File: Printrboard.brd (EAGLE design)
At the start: 100.1 x 61 mm, 122 parts, among them J1 MICROSD, J3 ATX, Q1 RFP30N06LE, Q2 RFP30N06LE, Q3 RFP30N06LE, U1 LM2841, U2 A4982, U3 A4982, U4 A4982, U5 A4982, U6 AT90USB1286, U7 AP7313, U8 TXB0104, X1 16MHz, X2 USB-MICROB

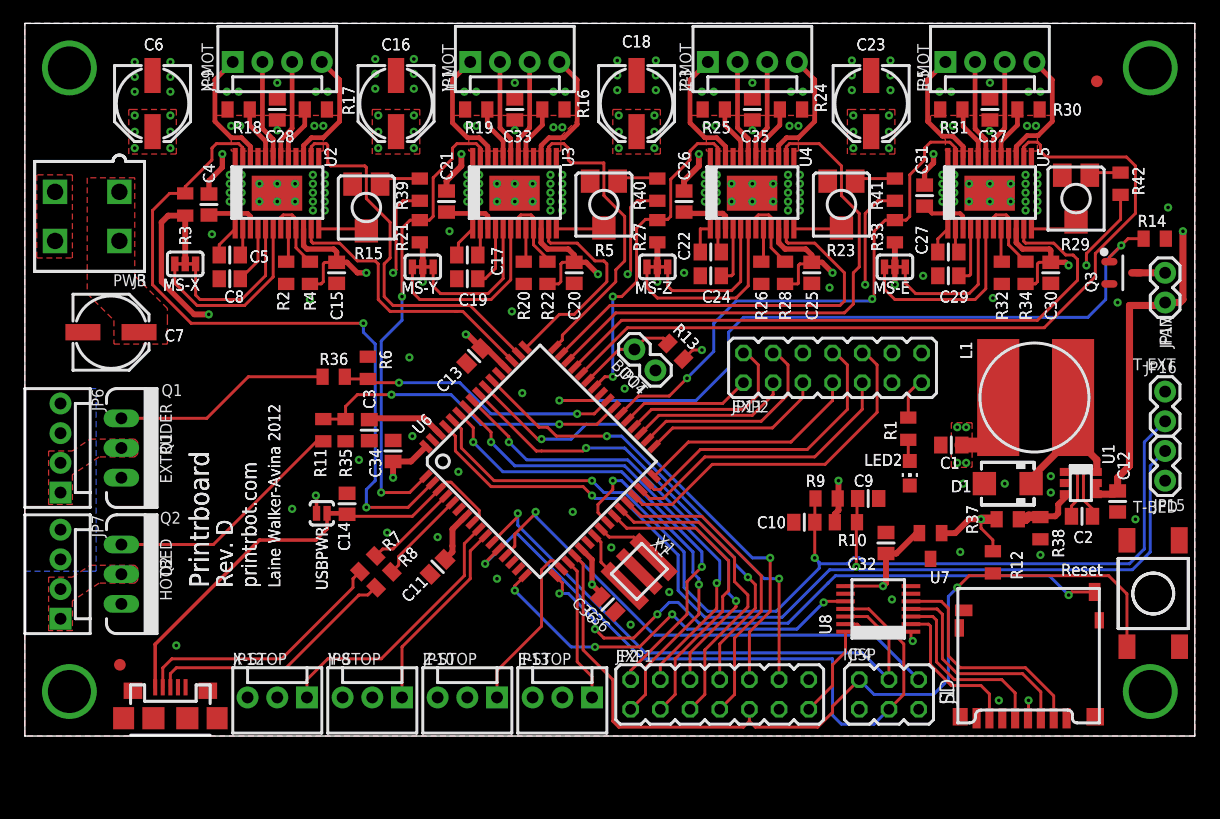
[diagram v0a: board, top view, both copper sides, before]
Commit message: Update files for Rev F
Changed heatbed connector to 5mm pitch screw terminal
Removed E-STOP connector
Changed Y-STOP pin
Moved former Y-STOP pin to SD interface to fix a limitation of the SPI ctlr
Added I2C connector
Replaced trimpots with 4-channel I2C DAC
Added polyfuse and reverse protection diode to fan circuit
Added more empty space around fan connector
Made ICSP and EXP1 connector pins share a 0.1" grid
Removed reset signal from EXP1, and replaced it with GPIO
Changed input PWR connector to a 6-pin one from the same family
Removed stop layer from several vias for future bed-of-nails tester
Change to through-hole mount microUSB connector
Added USB TVS diode pack to protect USB controller from ESD
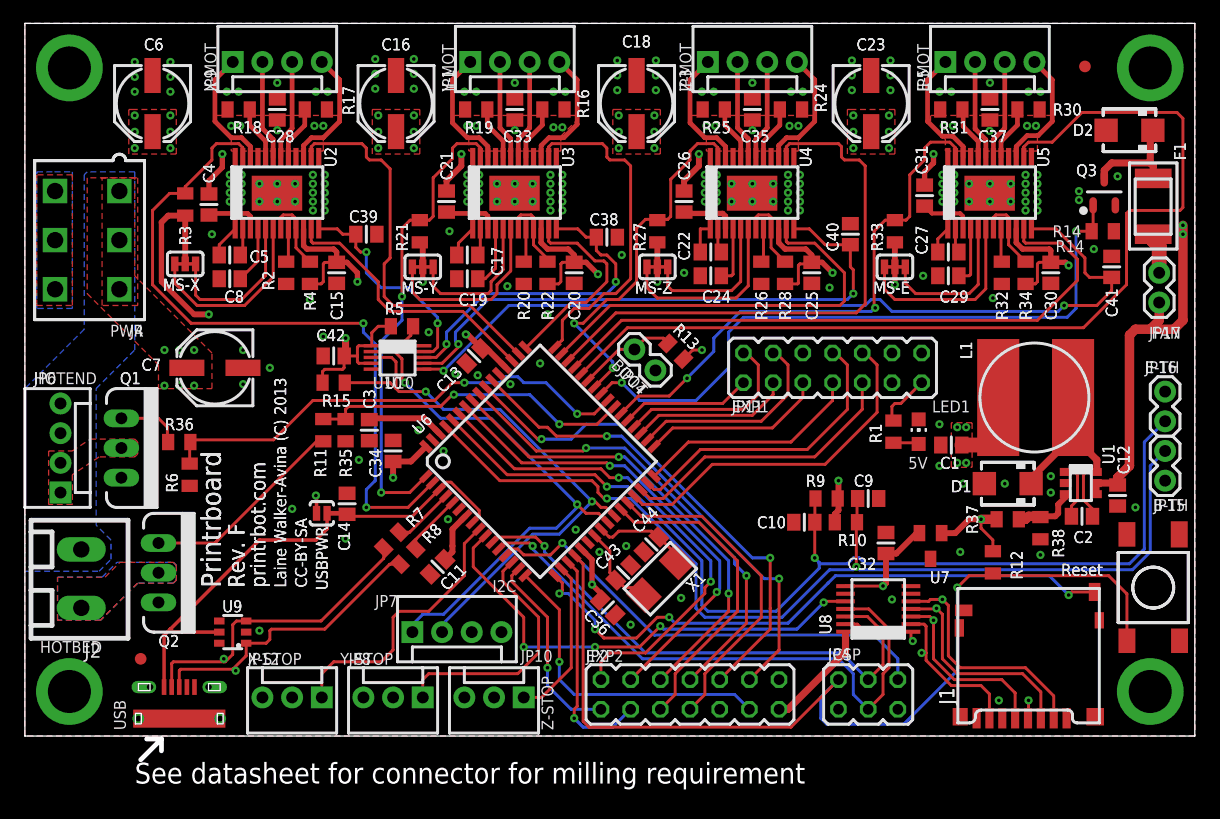
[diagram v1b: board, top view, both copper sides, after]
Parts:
- removed JP13: E-STOP, SparkFun:MOLEX-1X3
- removed LED2: PWR, led:CHIP-LED0805
- removed R23, R29: 10k, printrbot:RTRIM-ST4ETB
- removed R39, R40, R41, R42: 20k, ipc-7351-resistor:RESC2012X70N
- removed X2: USB-MICROB, printrbot:USB-MICROB
- added C38, C39, C40, C41, C42: 0.1uF, ipc-7351-capacitor:CAPC2012X145AN
- added C43, C44: 10pF, ipc-7351-capacitor:CAPC2012X145AN
- added D2: (no value), printrbot:SMA
- added F1: (no value), printrbot:MINISMDC
- added J2: (no value), printrbot:PHOENIX-5MM-2POS
- added J4: PCIE, printrbot:5566-6
- added LED1: PWR, led:CHIP-LED0805
- added U10: MCP4728, printrbot:MSOP10
- added U9: PRTR5V0U4D, printrbot:SOT23-6
- J3: value ATX -> USB-MICRO-PTH; device printrbot:5566-4 -> printrbot:USB-MICROB-PTH
- JP7: value HOTBED -> I2C
- R15, R5: value 10k -> 4.7k; device printrbot:RTRIM-ST4ETB -> ipc-7351-resistor:RESC2012X70N
- X1: device printrbot:AWSCR -> printrbot:NDK-XTAL
- moved J3 42.9 mm to (13.2, 2.29), turned to 0 degrees
- moved JP7 30.1 mm to (33.1, 8.89), turned to 0 degrees
- moved R5 20.2 mm to (32.3, 35.1)
- moved R6 17.8 mm to (14.1, 22.4), turned to 270 degrees
- moved R15 15.2 mm to (26.4, 30.2)
- moved R36 14.3 mm to (13.2, 25.1)
- moved C7 9.40 mm to (16.3, 31.5), turned to 180 degrees
- moved Q3 7.10 mm to (92.3, 46.5), turned to 90 degrees
- moved R14 4.49 mm to (92.2, 43.2)
- moved Q2 3.18 mm to (11.4, 14.0)
- moved R7 2.87 mm to (31.4, 16.8)
- moved R8 2.86 mm to (32.8, 15.4)
- moved JP2 2.54 mm to (56.9, 3.56)
- moved JP10 2.29 mm to (42.7, 3.30)
- moved X1 1.90 mm to (54.4, 13.5)
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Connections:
- removed net E-STOP: JP13.1, U6.19
- removed net N$18: R15.W, U2.12
- removed net N$33: R5.W, U3.12
- removed net N$48: R23.W, U4.12
- removed net N$6: JP17.2, Q3.3
- removed net N$63: R29.W, U5.12
- removed net N$69: R15.1, R39.1
- removed net N$74: R29.1, R42.1
- removed net N$78: R23.1, R41.1
- removed net N$8: R40.1, R5.1
- removed net PD0-SCL: JP2.1, U6.25
- removed net PD1-SDA: JP2.3, U6.26
- new net MCU_DN: J3.D-, R7.1, U9.3
- new net MCU_DP: J3.D+, R8.1, U9.1
- new net PB5: JP2.1, U6.15
- new net PB6: JP2.11, U6.16
- new net PE5: JP2.3, U6.19
- new net SCL: JP7.1, R5.1, U10.2, U6.25
- new net SDA: JP7.2, R15.1, U10.3, U6.26
- new net VREF_E: C41.1, U10.6, U5.12
- new net VREF_X: C39.1, U10.9, U2.12
- new net VREF_Y: C38.1, U10.8, U3.12
- new net VREF_Z: C40.1, U10.7, U4.12
- net !RESET: no longer JP2.9
- net +5V: now also C42.2, JP7.4, R15.2, R5.2, U10.1, U10.4; no longer JP13.2, R39.2, R40.2, R41.2, R42.2
- net 12V: now also J2.P$1, J4.1, J4.2, J4.3; no longer J3.1, J3.2, JP7.3, JP7.4
- net GND: now also C38.2, C39.2, C40.2, C41.2, C42.1, C43.1, C44.1, D2.A, J3.GND, J3.GND1, J3.GND2, J3.GND3, J3.GND4, J3.GND5, J4.4, J4.5, J4.6, JP7.3, LED1.C, U10.10, U9.2; no longer J3.3, J3.4, JP13.3, LED2.C, R15.2, R23.2, R29.2, R5.2, X1.GND, X2.GND, X2.MT1, X2.MT2, X2.MT3, X2.MT4, X2.MT5, X2.MT6
- net HOTBED-GND: now also J2.P$2; no longer JP7.1, JP7.2
- net N$1: now also LED1.A; no longer LED2.A
- net N$2: now also D2.C, F1.P$2, Q3.3; no longer R7.1, X2.D-
- net N$5: now also F1.P$1, JP17.2; no longer R8.1, X2.D+
- net SDCS: now also U6.10; no longer U6.16
- net VBUS: now also J3.VBUS, U9.5; no longer X2.VBUS
- net XTAL1: now also C44.2, X1.P$1; no longer X1.IN
- net XTAL2: now also C43.2, X1.P$2; no longer X1.OUT
- net Y-STOP: now also U6.14; no longer U6.10
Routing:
- net VREF_E: track 0.00 -> 73.2 mm, vias 0 -> 2
- net SDA: track 0.00 -> 50.1 mm, vias 0 -> 2
- net VREF_Z: track 0.00 -> 50.0 mm, vias 0 -> 2
- net SCL: track 0.00 -> 49.3 mm, vias 0 -> 2
- net PD0-SCL: track 29.9 -> 0.00 mm, vias 2 -> 0
- net VREF_Y: track 0.00 -> 28.6 mm, vias 0 -> 2
- net PB6: track 0.00 -> 27.4 mm, vias 0 -> 1
- net MCU_DN: track 0.00 -> 26.5 mm, vias 0 -> 1
- net PD1-SDA: track 26.5 -> 0.00 mm
- net MCU_DP: track 0.00 -> 25.5 mm, vias 0 -> 1
- net PE5: track 0.00 -> 19.5 mm, vias 0 -> 1
- net VREF_X: track 0.00 -> 18.9 mm, vias 0 -> 2
- net N$5: track 21.8 -> 3.51 mm
- net !HOTEND: track 24.7 -> 42.2 mm
- net PB5: track 0.00 -> 16.9 mm, vias 0 -> 1
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- added copper zone on layer 16, net HOTBED-GND
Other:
- board size 100.1 x 61 mm -> 100.1 x 63 mm
- board text added: "/home/ceriand/Downloads/pbrd-logo.bmp"
- board text added: "5V"
- board text added: "B-TH"
- board text added: "C38"
- board text added: "C39"
- board text added: "C40"
- board text added: "C41"
- board text added: "C42"
- board text added: "C43"
- board text added: "C44"
- board text added: "CC-BY-SA"
- board text added: "D2"
- board text added: "E-TH"
- board text added: "F1"
- board text added: "HOTEND"
- board text added: "I2C"
- board text added: "J1"
- board text added: "Laine Walker-Avina (C) 2013"
- board text added: "Rev. F"
- board text added: "See datasheet for connector for milling requirement"
- board text added: "U10"
- board text added: "U9"
- board text added: "USB"
- board text removed: "E-STOP"
- board text removed: "EXTRUDER"
- board text removed: "LED2"
- board text removed: "Laine Walker-Avina 2012"
- board text removed: "R23"
- board text removed: "R29"
- board text removed: "R39"
- board text removed: "R40"
- board text removed: "R41"
- board text removed: "R42"
- board text removed: "Rev. D"
- board text removed: "SD"
- board text removed: "T-BED"
- board text removed: "T-EXT"

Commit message: Manufacturability changes
Added some pin 1 indicators
Added test point for VBUS signal
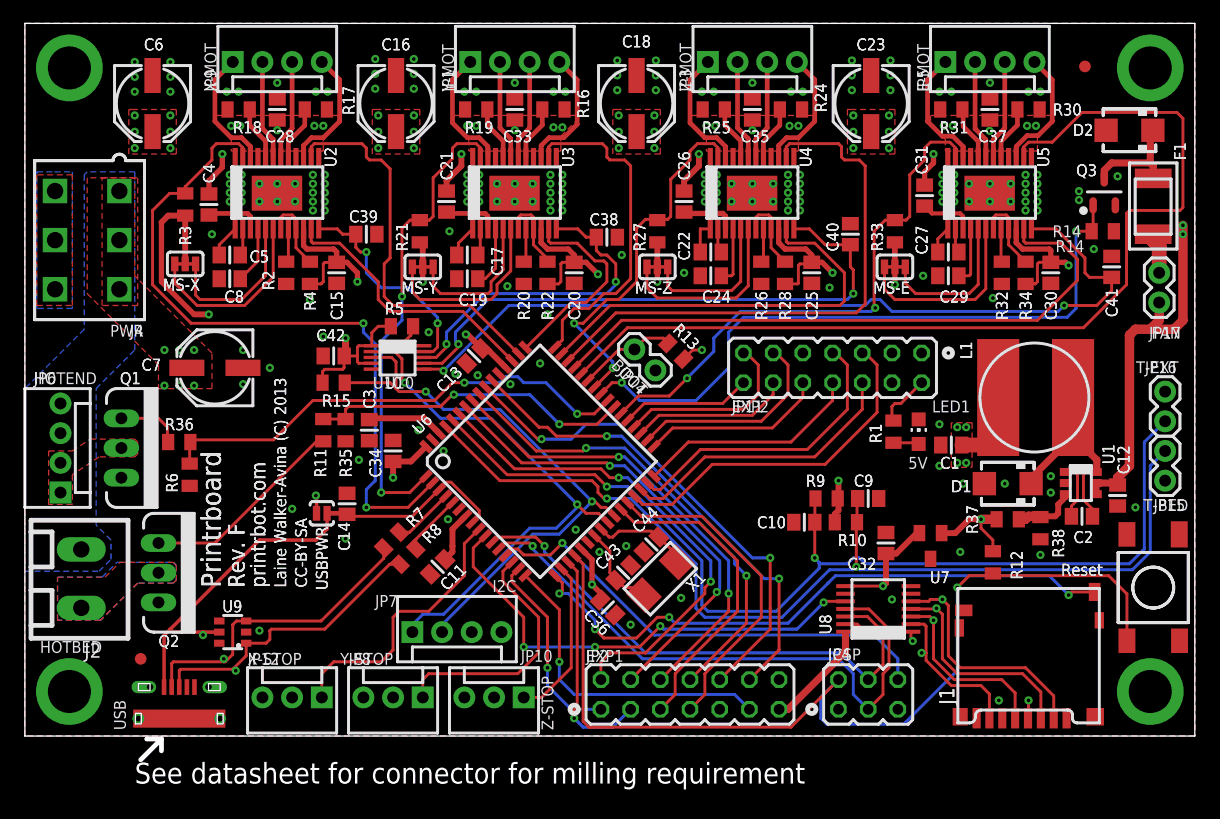
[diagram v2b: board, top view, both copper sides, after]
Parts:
- JP11: value EXP -> EXP2
- JP2: value EXP -> EXP1
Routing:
- net VBUS: track 44.4 -> 44.7 mm, vias 0 -> 1
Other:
- board text added: "T-BED"
- board text added: "T-EXT"
- board text removed: "B-TH"
- board text removed: "E-TH"
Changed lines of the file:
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@@
 <layer number="14" name="Route14" color="1" fill="6" visible="no" active="no"/>
 <layer number="15" name="Route15" color="4" fill="6" visible="no" active="no"/>
-<layer number="16" name="Bottom" color="1" fill="1" visible="yes" active="yes"/>
+<layer number="16" name="Bottom" color="1" fill="1" visible="no" active="yes"/>
 <layer number="17" name="Pads" color="2" fill="1" visible="yes" active="yes"/>
 <layer number="18" name="Vias" color="2" fill="1" visible="yes" active="yes"/>
@@
 <wire x1="60.706" y1="5.715" x2="61.087" y2="6.096" width="0.254" layer="121"/>
 <wire x1="63.246" y1="5.715" x2="63.627" y2="6.096" width="0.254" layer="121"/>
-<text x="48.006" y="6.35" size="1.016" layer="121" ratio="25">EXP2</text>
+<text x="48.006" y="6.35" size="1.016" layer="121" ratio="25">EXP1</text>
 <wire x1="57.15" y1="60.706" x2="57.15" y2="55.118" width="0.254" layer="121"/>
 <wire x1="67.31" y1="60.706" x2="67.31" y2="55.118" width="0.254" layer="121"/>
@@
 <wire x1="65.278" y1="29.337" x2="64.897" y2="28.956" width="0.254" layer="121"/>
 <wire x1="62.738" y1="29.337" x2="62.357" y2="28.956" width="0.254" layer="121"/>
-<text x="60.452" y="27.686" size="1.016" layer="121" ratio="25">EXP1</text>
+<text x="60.452" y="27.686" size="1.016" layer="121" ratio="25">EXP2</text>
 <wire x1="26.67" y1="0.254" x2="26.67" y2="5.842" width="0.254" layer="121"/>
 <wire x1="19.05" y1="0.254" x2="19.05" y2="5.842" width="0.254" layer="121"/>
@@
 <wire x1="96.266" y1="23.749" x2="96.266" y2="25.019" width="0.254" layer="121"/>
 <wire x1="98.171" y1="20.574" x2="96.901" y2="20.574" width="0.254" layer="121"/>
-<text x="99.5172" y="20.2692" size="1.016" layer="121" ratio="25" rot="R180">B-TH</text>
+<text x="99.5172" y="20.2692" size="1.016" layer="121" ratio="25" rot="R180">T-BED</text>
 <wire x1="96.266" y1="26.289" x2="96.266" y2="27.559" width="0.254" layer="121"/>
 <wire x1="96.266" y1="27.559" x2="96.901" y2="28.194" width="0.254" layer="121"/>
@@
 <wire x1="98.806" y1="27.559" x2="98.806" y2="26.289" width="0.254" layer="121"/>
 <wire x1="96.901" y1="30.734" x2="98.171" y2="30.734" width="0.254" layer="121"/>
-<text x="95.8088" y="31.0388" size="1.016" layer="121" ratio="25">E-TH</text>
+<text x="95.0468" y="31.0388" size="1.016" layer="121" ratio="25">T-EXT</text>
 <wire x1="95.758" y1="36.449" x2="95.758" y2="37.719" width="0.254" layer="121"/>
 <wire x1="95.758" y1="37.719" x2="96.393" y2="38.354" width="0.254" layer="121"/>
@@
 <wire x1="11.684" y1="-0.254" x2="11.684" y2="-1.27" width="0.4064" layer="46"/>
 <text x="8.636" y="0.508" size="1.016" layer="121" ratio="20" rot="R90">USB</text>
+<circle x="46.99" y="2.286" radius="0.359209375" width="0.4064" layer="121"/>
+<circle x="78.994" y="32.766" radius="0.359209375" width="0.4064" layer="121"/>
+<circle x="67.31" y="2.286" radius="0.359209375" width="0.4064" layer="121"/>
 </plain>
 <attributes>
@@
 <attribute name="VALUE" x="43.942" y="7.747" size="1.27" layer="27" rot="R180"/>
 </element>
-<element name="JP2" library="printrbot" package="JP7Q" value="EXP" x="56.896" y="3.556" smashed="yes">
+<element name="JP2" library="printrbot" package="JP7Q" value="EXP1" x="56.896" y="3.556" smashed="yes">
 <attribute name="NAME" x="48.006" y="6.35" size="1.016" layer="25" ratio="20"/>
 <attribute name="VALUE" x="48.006" y="-2.159" size="1.27" layer="27" ratio="10"/>
 </element>
-<element name="JP11" library="printrbot" package="JP7Q" value="EXP" x="69.088" y="31.496" smashed="yes" rot="R180">
+<element name="JP11" library="printrbot" package="JP7Q" value="EXP2" x="69.088" y="31.496" smashed="yes" rot="R180">
 <attribute name="NAME" x="60.452" y="27.686" size="1.016" layer="25" ratio="20"/>
 <attribute name="VALUE" x="77.978" y="37.211" size="1.27" layer="27" ratio="10" rot="R180"/>
@@
 <contactref element="J3" pad="VBUS"/>
 <contactref element="U9" pad="5"/>
-<wire x1="16.63" y1="8.89" x2="12.7" y2="8.89" width="0.3048" layer="1"/>
+<wire x1="16.63" y1="8.89" x2="15.24" y2="8.89" width="0.3048" layer="1"/>
+<wire x1="15.24" y1="8.89" x2="12.7" y2="8.89" width="0.3048" layer="1"/>
 <wire x1="12.7" y1="8.89" x2="12.446" y2="9.144" width="0.3048" layer="1"/>
 <wire x1="11.908" y1="4.191" x2="11.908" y2="8.606" width="0.3048" layer="1"/>
 <wire x1="11.908" y1="8.606" x2="12.446" y2="9.144" width="0.3048" layer="1"/>
+<via x="15.24" y="8.636" extent="1-16" drill="0.3048" alwaysstop="yes"/>
+<wire x1="15.24" y1="8.636" x2="15.24" y2="8.89" width="0.3048" layer="1"/>
 </signal>
 <signal name="SDCS">

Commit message: Redraw USB connector for manufacturability
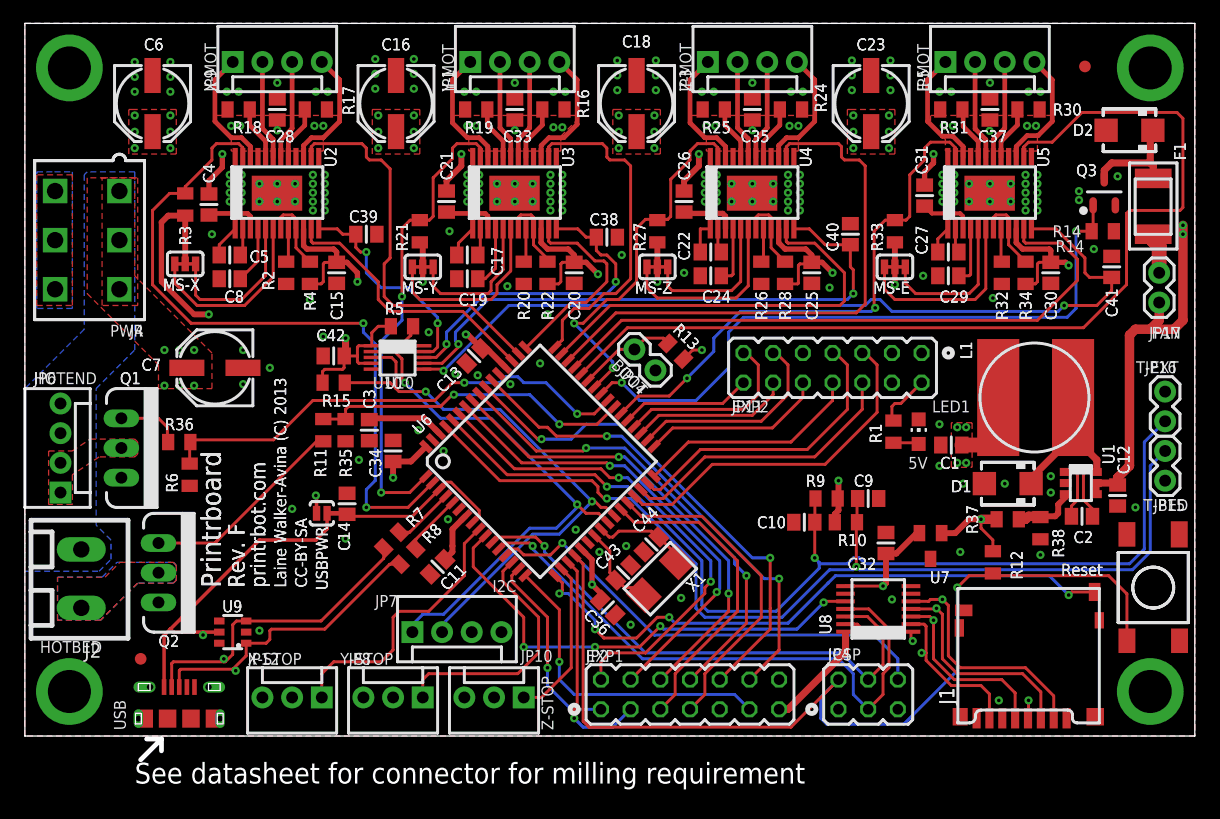
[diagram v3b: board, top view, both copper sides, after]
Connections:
- net GND: now also J3.GND6, J3.GND7, J3.GND8
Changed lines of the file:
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@@
 <?xml version="1.0" encoding="utf-8"?>
 <!DOCTYPE eagle SYSTEM "eagle.dtd">
-<eagle version="6.1">
+<eagle version="6.6.0">
 <drawing>
 <settings>
@@
 <grid distance="10" unitdist="mil" unit="mil" style="lines" multiple="1" display="yes" altdistance="5" altunitdist="mil" altunit="mil"/>
 <layers>
-<layer number="1" name="Top" color="4" fill="1" visible="no" active="yes"/>
+<layer number="1" name="Top" color="4" fill="1" visible="yes" active="yes"/>
 <layer number="2" name="PWR" color="16" fill="1" visible="no" active="yes"/>
 <layer number="3" name="GND" color="17" fill="1" visible="no" active="yes"/>
@@
 <layer number="14" name="Route14" color="1" fill="6" visible="no" active="no"/>
 <layer number="15" name="Route15" color="4" fill="6" visible="no" active="no"/>
-<layer number="16" name="Bottom" color="1" fill="1" visible="no" active="yes"/>
+<layer number="16" name="Bottom" color="1" fill="1" visible="yes" active="yes"/>
 <layer number="17" name="Pads" color="2" fill="1" visible="yes" active="yes"/>
 <layer number="18" name="Vias" color="2" fill="1" visible="yes" active="yes"/>
@@
 </class>
 </classes>
-<designrules>
+<designrules name="4pcb">
 <description language="de">&lt;b&gt;EAGLE Design Rules&lt;/b&gt;
 &lt;p&gt;
@@
 <param name="rvMicroViaOuter" value="0.25"/>
 <param name="rvMicroViaInner" value="0.25"/>
-<param name="rlMinPadTop" value="10mil"/>
+<param name="rlMinPadTop" value="6mil"/>
 <param name="rlMaxPadTop" value="20mil"/>
-<param name="rlMinPadInner" value="10mil"/>
+<param name="rlMinPadInner" value="6mil"/>
 <param name="rlMaxPadInner" value="20mil"/>
-<param name="rlMinPadBottom" value="10mil"/>
+<param name="rlMinPadBottom" value="6mil"/>
 <param name="rlMaxPadBottom" value="20mil"/>
 <param name="rlMinViaOuter" value="8mil"/>
@@
 <param name="mvStopFrame" value="1"/>
 <param name="mvCreamFrame" value="0"/>
-<param name="mlMinStopFrame" value="2mil"/>
-<param name="mlMaxStopFrame" value="3mil"/>
+<param name="mlMinStopFrame" value="6mil"/>
+<param name="mlMaxStopFrame" value="6mil"/>
 <param name="mlMinCreamFrame" value="0mil"/>
 <param name="mlMaxCreamFrame" value="0mil"/>
@@
 <contactref element="J4" pad="4"/>
 <contactref element="U9" pad="2"/>
-<contactref element="J3" pad="GND2"/>
 <contactref element="J3" pad="GND5"/>
-<contactref element="J3" pad="GND3"/>
 <contactref element="J3" pad="GND"/>
 <contactref element="J3" pad="GND4"/>
-<contactref element="J3" pad="GND1"/>
 <contactref element="U10" pad="10"/>
 <via x="91.44" y="41.656" extent="1-16" drill="0.3048"/>
@@
 <vertex x="1.016" y="48.26"/>
 </polygon>
+<contactref element="J3" pad="GND1"/>
+<contactref element="J3" pad="GND2"/>
+<contactref element="J3" pad="GND3"/>
+<contactref element="J3" pad="GND6"/>
+<contactref element="J3" pad="GND7"/>
+<contactref element="J3" pad="GND8"/>
 </signal>
 <signal name="!RESET">
@@
 <vertex x="5.08" y="34.798"/>
 <vertex x="0" y="29.718"/>
-<vertex x="0" y="29.718"/>
 <vertex x="0" y="14.097"/>
 <vertex x="6.35" y="14.097"/>
@@
 <vertex x="100.076" y="41.91"/>
 <vertex x="14.986" y="41.91"/>
-<vertex x="14.986" y="0"/>
+<vertex x="14.986" y="5.334"/>
+<vertex x="17.78" y="5.334"/>
+<vertex x="17.78" y="0"/>
 <vertex x="77.597" y="0"/>
 <vertex x="77.597" y="6.985"/>
